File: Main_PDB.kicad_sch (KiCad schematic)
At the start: 124 parts, among them J1 Conn_01x02_MountingPin, J10 Conn_01x02_MountingPin, J12 Conn_01x02_MountingPin, J2 Conn_01x02_MountingPin, J3 Conn_01x02_MountingPin, J4 Conn_01x02_MountingPin, J5 Conn_01x02_MountingPin, J6 Conn_01x01_MountingPin, J7 Conn_01x01_MountingPin, J8 Conn_01x09_MountingPin, J9 Conn_01x03_MountingPin, Q1 PMOS, Q10 NMOS, Q14 NMOS, Q15 NMOS, Q2 NPN, Q7 NMOS, Q8 NMOS, Q9 NMOS, U1 LRM36015, U10 LM5148RGYR, U11 ACS758LCB-100U-PFF-T, U12 TPS48110AQDGXRQ1, U13 LM5148RGYR, U14 UCC27511DBVR, U2 ACS758LCB-100U-PFF-T, U4 ACS758LCB-100U-PFF-T, U5 ACS758LCB-100U-PFF-T, U6 ACS758LCB-100U-PFF-T, U8 ACS758LCB-100U-PFF-T, U9 ACS758LCB-100U-PFF-T

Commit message: Changed 48->24 to 48->12
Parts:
- C14: value 30u -> 83u
- C2: value 15u -> 285u
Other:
- moved on the sheet: D7
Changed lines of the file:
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@@
 	)
 	(junction
-		(at 505.46 388.62)
+		(at 166.37 243.84)
 		(diameter 0)
 		(color 0 0 0 0)
 	)
 	(junction
-		(at 166.37 243.84)
+		(at 504.19 388.62)
 		(diameter 0)
 		(color 0 0 0 0)
@@
 	(wire
 		(pts
-			(xy 505.46 388.62) (xy 510.54 388.62)
-		)
-		(stroke
-			(width 0)
-			(type default)
-		)
-	)
-	(wire
-		(pts
 			(xy 64.77 138.43) (xy 64.77 114.3)
 		)
@@
 	(wire
 		(pts
-			(xy 499.11 388.62) (xy 505.46 388.62)
+			(xy 499.11 388.62) (xy 504.19 388.62)
 		)
 		(stroke
@@
 	(wire
 		(pts
+			(xy 504.19 388.62) (xy 510.54 388.62)
+		)
+		(stroke
+			(width 0)
+			(type default)
+		)
+	)
+	(wire
+		(pts
 			(xy 34.29 99.06) (xy 68.58 99.06)
 		)
@@
 	(symbol
 		(lib_id "Device:D_Zener")
-		(at 505.46 384.81 90)
+		(at 504.19 384.81 90)
 		(unit 1)
 		(body_style 1)
@@
 		(dnp no)
 		(property "Reference" "D7"
-			(at 509.27 382.27 90)
+			(at 508 382.27 90)
 			(show_name no)
 			(do_not_autoplace no)
@@
 		)
 		(property "Value" "TVS"
-			(at 509.27 384.81 90)
+			(at 508 384.81 90)
 			(show_name no)
 			(do_not_autoplace no)
@@
 		)
 		(property "Footprint" ""
-			(at 505.46 384.81 0)
+			(at 504.19 384.81 0)
 			(hide yes)
 			(show_name no)
@@
 		)
 		(property "Datasheet" ""
-			(at 505.46 384.81 0)
+			(at 504.19 384.81 0)
 			(hide yes)
 			(show_name no)
@@
 		)
 		(property "Description" "Zener diode"
-			(at 505.46 384.81 0)
+			(at 504.19 384.81 0)
 			(hide yes)
 			(show_name no)
@@
 	(symbol
 		(lib_id "power:GND")
-		(at 505.46 381 180)
+		(at 504.19 381 180)
 		(unit 1)
 		(body_style 1)
@@
 		(fields_autoplaced yes)
 		(property "Reference" "#PWR054"
-			(at 505.46 374.65 0)
+			(at 504.19 374.65 0)
 			(hide yes)
 			(show_name no)
@@
 		)
 		(property "Value" "GND"
-			(at 505.4601 377.19 90)
+			(at 504.1901 377.19 90)
 			(show_name no)
 			(do_not_autoplace no)
@@
 		)
 		(property "Footprint" ""
-			(at 505.46 381 0)
+			(at 504.19 381 0)
 			(hide yes)
 			(show_name no)
@@
 		)
 		(property "Datasheet" ""
-			(at 505.46 381 0)
+			(at 504.19 381 0)
 			(hide yes)
 			(show_name no)
@@
 		)
 		(property "Description" "Power symbol creates a global label with name \"GND\" , ground"
-			(at 505.46 381 0)
+			(at 504.19 381 0)
 			(hide yes)
 			(show_name no)
@@
 			)
 		)
-		(property "Value" "15u"
+		(property "Value" "285u"
 			(at 335.28 351.7899 0)
 			(show_name no)
@@
 			)
 		)
-		(property "Value" "30u"
+		(property "Value" "83u"
 			(at 502.92 393.6999 0)
 			(show_name no)
@@
 		(dnp no)
 		(property "Reference" "Q7"
-			(at 85.09 40.64 90)
+			(at 85.344 54.356 90)
 			(show_name no)
 			(do_not_autoplace no)

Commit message: Format change
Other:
- note added: "48V to 12V buck + current sensor"
- note removed: "48V to 24V buck + current sensor"
- moved on the sheet: C1, C10, C11, C12, C13, C14, C19, C2, C20, C21, C22, C23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

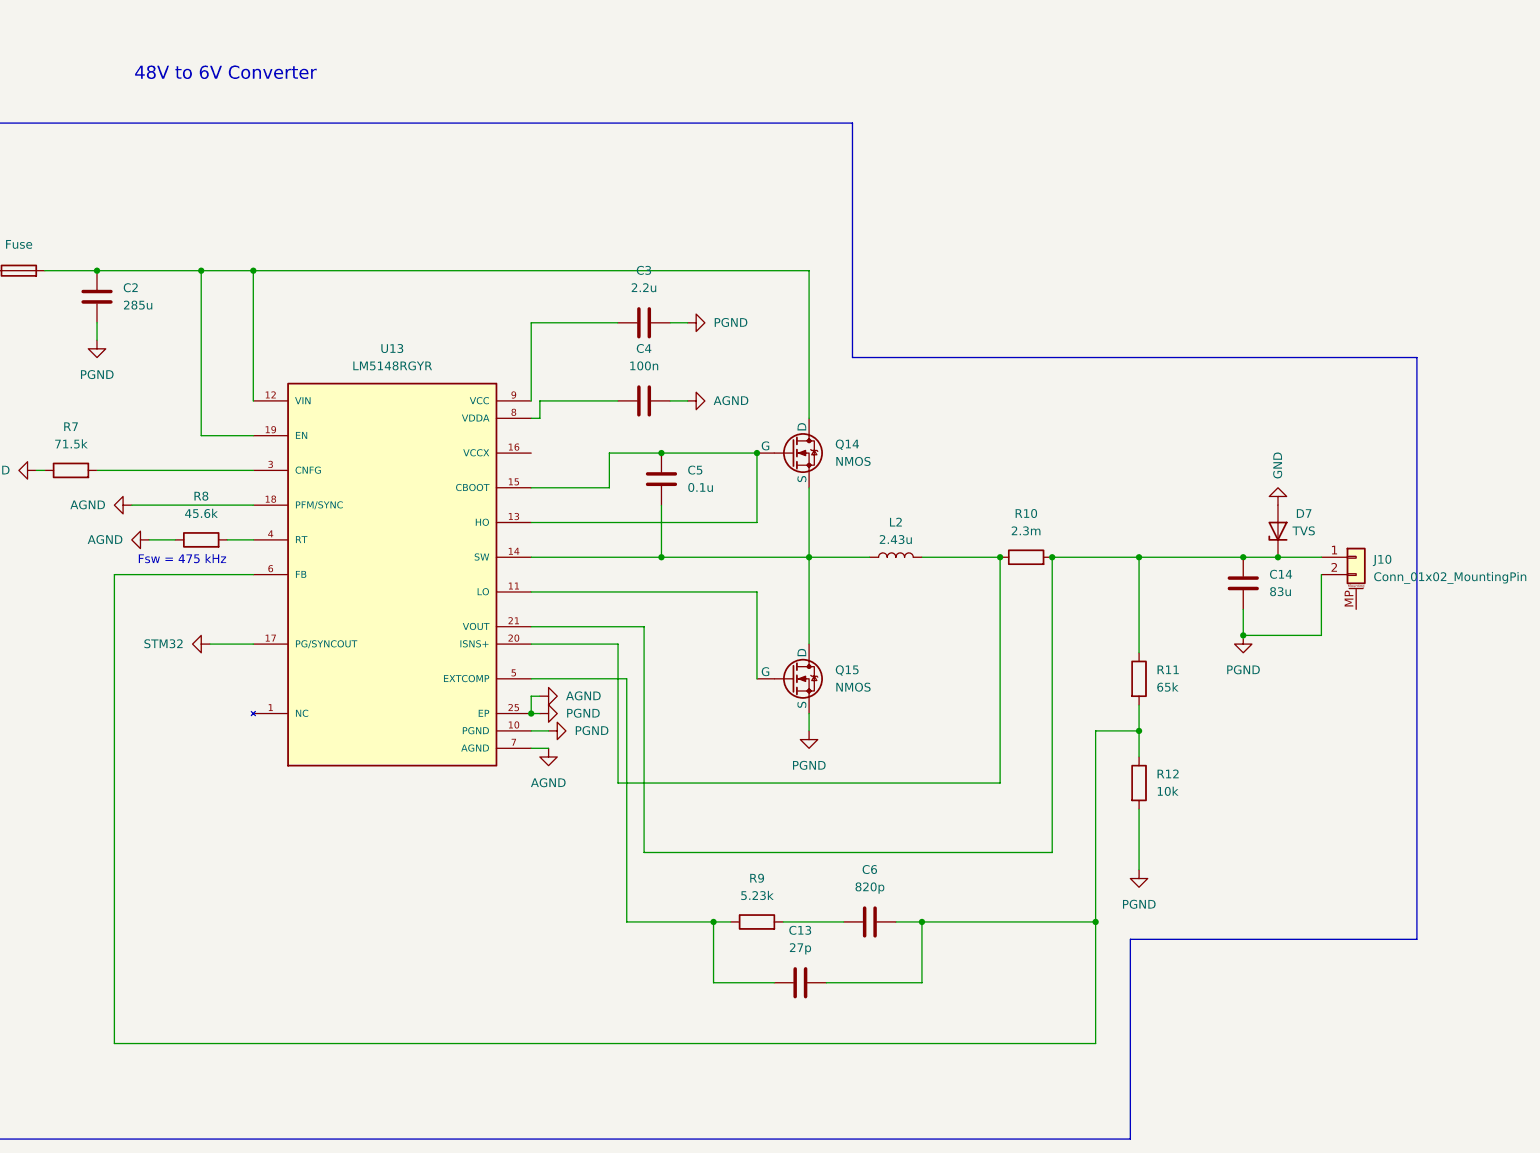
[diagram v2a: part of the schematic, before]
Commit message: updated component values for 6v convert
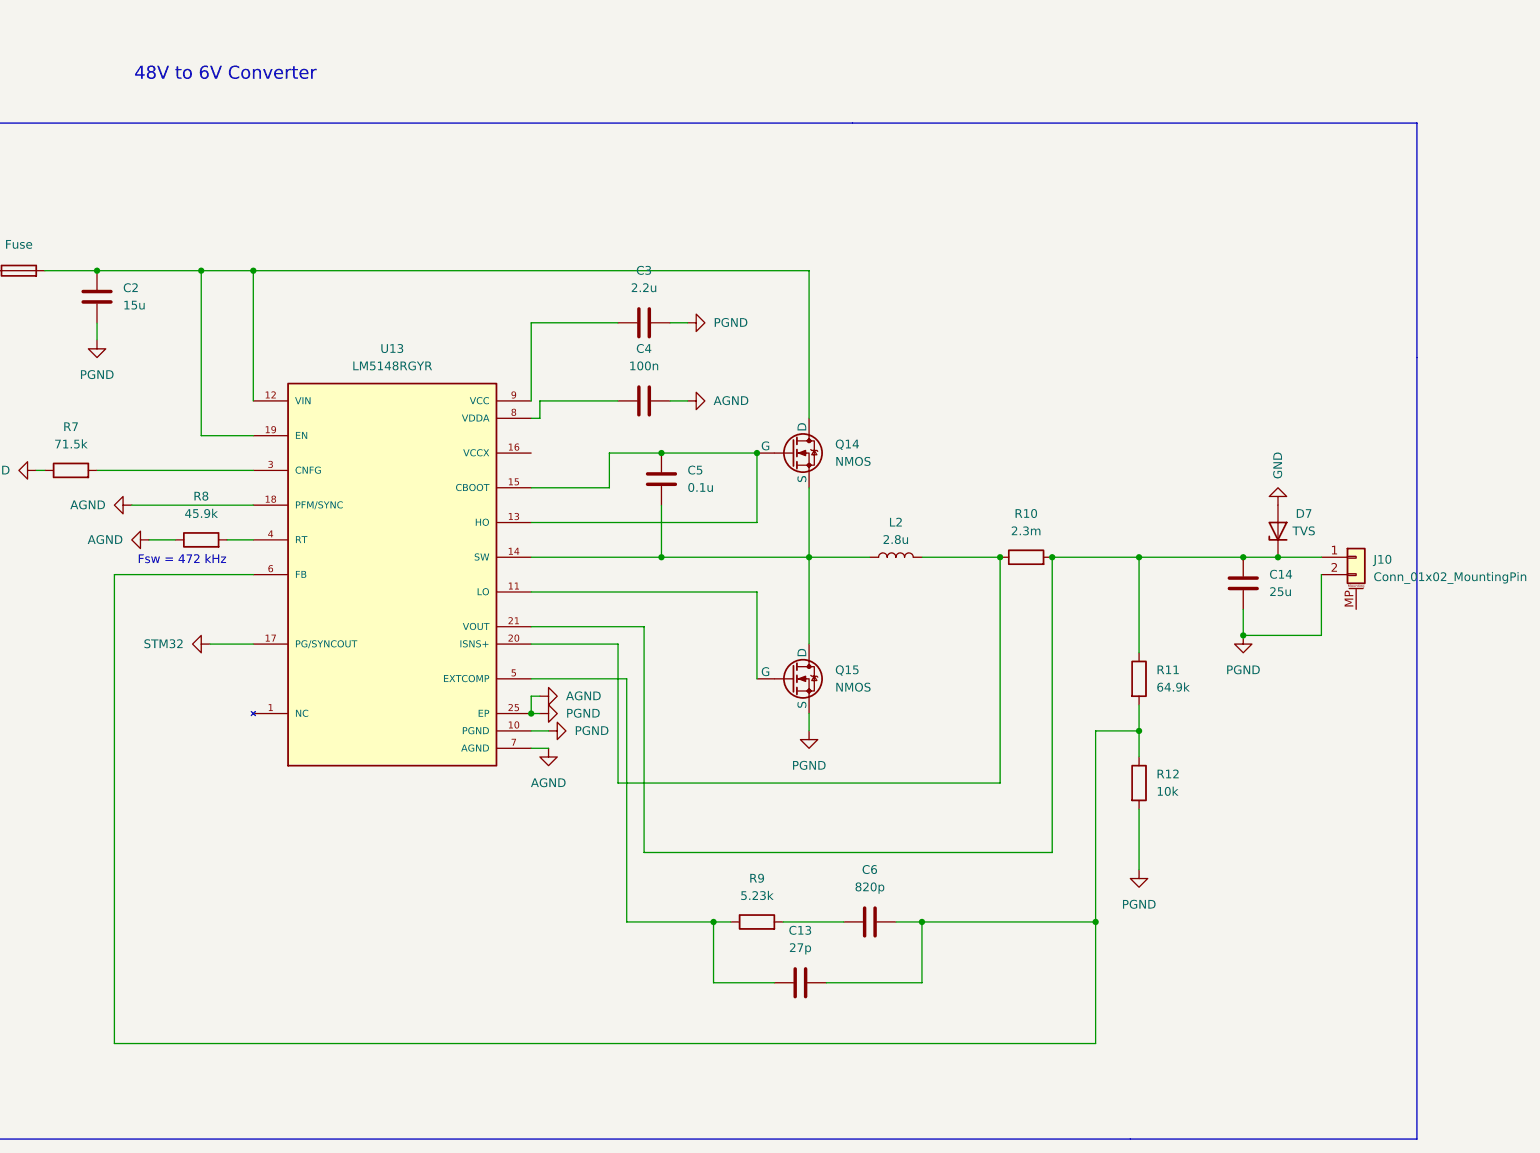
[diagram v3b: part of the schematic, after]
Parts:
- C14: value 83u -> 25u
- C2: value 285u -> 15u
- L2: value 2.43u -> 2.8u
- R11: value 65k -> 64.9k
- R8: value 45.6k -> 45.9k
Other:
- note added: "Fsw = 472 kHz"
- note removed: "Fsw = 475 kHz"
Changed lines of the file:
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@@
 		)
 	)
-	(text "Fsw = 475 kHz"
+	(text "Fsw = 472 kHz"
 		(exclude_from_sim no)
 		(at 553.466 399.288 0)
@@
 	(polyline
 		(pts
-			(xy 692.15 483.87) (xy 692.15 454.66)
+			(xy 692.15 483.87) (xy 692.15 483.87)
 		)
 		(stroke
@@
 	(polyline
 		(pts
-			(xy 692.15 454.66) (xy 734.06 454.66)
+			(xy 692.15 483.87) (xy 734.06 483.87)
 		)
 		(stroke
@@
 	(polyline
 		(pts
-			(xy 734.06 369.57) (xy 651.51 369.57)
+			(xy 734.06 369.57) (xy 734.06 335.28)
 		)
 		(stroke
@@
 	(polyline
 		(pts
-			(xy 734.06 454.66) (xy 734.06 369.57)
+			(xy 734.06 483.87) (xy 734.06 369.57)
 		)
 		(stroke
@@
 	(polyline
 		(pts
-			(xy 651.51 369.57) (xy 651.51 335.28)
+			(xy 734.06 335.28) (xy 651.51 335.28)
 		)
 		(stroke
@@
 			)
 		)
-		(property "Value" "65k"
+		(property "Value" "64.9k"
 			(at 695.96 417.8299 0)
 			(show_name no)
@@
 			)
 		)
-		(property "Value" "45.6k"
+		(property "Value" "45.9k"
 			(at 556.26 392.43 90)
 			(show_name no)
@@
 			)
 		)
-		(property "Value" "2.43u"
+		(property "Value" "2.8u"
 			(at 657.86 396.24 90)
 			(show_name no)
@@
 			)
 		)
-		(property "Value" "285u"
+		(property "Value" "15u"
 			(at 544.83 361.9499 0)
 			(show_name no)
@@
 			)
 		)
-		(property "Value" "83u"
+		(property "Value" "25u"
 			(at 712.47 403.8599 0)
 			(show_name no)

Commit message: updated grounds for converters, need to double check grounds for current sense. Did not adjust grounds on actuators/precharge. Added pull up resistor on 6v PG output.
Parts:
- added R4: PullUpRes, symbol Device:R
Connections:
- net AGND: now also C26.2, C27.2, C28.2, C29.2, C30.2, C31.2, C33.2, C38.2, C39.2, C40.2, C41.2, C45.2, C46.2, C47.2, C48.2, C49.2, CHF1.2, CHF2.2, CIN1.2, COUT1.2, COUT2.2, CVCC1.1, J1.2 (Pin_2), J12.2 (Pin_2), Q9.3 (S), R17.1, R18.1, R21.2, RFBB1.1, U1.1 (PGND), U1.11 (PGND), U1.6 (AGND), U10.10 (PGND), U10.16 (VCCX), U10.17 (PG/SYNCOUT), U10.18 (PFM/SYNC), U10.25 (EP), U10.7 (AGND), U11.2 (GND), U9.2 (GND)
- net GND: no longer C26.2, C27.2, C28.2, C29.2, C30.2, C31.2, C38.2, C39.2, C40.2, C41.2, C43.2, C44.2, C45.2, C46.2, C48.2, C49.2, CHF1.2, CHF2.2, CIN1.2, COUT1.2, COUT2.2, CVCC1.1, J1.2 (Pin_2), J12.2 (Pin_2), Q9.3 (S), R17.1, R18.1, R21.2, RFBB1.1, U1.1 (PGND), U1.11 (PGND), U1.6 (AGND), U10.10 (PGND), U10.16 (VCCX), U10.17 (PG/SYNCOUT), U10.18 (PFM/SYNC), U10.25 (EP), U10.7 (AGND)
- net GND1: no longer C33.2, C47.2, U11.2 (GND), U9.2 (GND)
- net STM32: now also R4.1; no longer U13.17 (PG/SYNCOUT)
- net at R20.2, R21.1, U10.6 (FB): now also C43.2, C44.2
- new net: R4.2, U13.17 (PG/SYNCOUT)
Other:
- moved on the sheet: R7

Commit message: changed ground for ext comp circuit
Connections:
- net AGND: now also C13.2, C43.2, C44.2, C6.2
- net at R11.2, R12.1, U13.6 (FB): no longer C13.2, C6.2
- net at R20.2, R21.1, U10.6 (FB): no longer C43.2, C44.2
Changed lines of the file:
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@@
 	)
 	(junction
+		(at 213.36 435.61)
+		(diameter 0)
+		(color 0 0 0 0)
+	)
+	(junction
 		(at 185.42 176.53)
 		(diameter 0)
@@
 	)
 	(junction
-		(at 260.35 443.23)
-		(diameter 0)
-		(color 0 0 0 0)
-	)
-	(junction
 		(at 196.85 440.69)
 		(diameter 0)
@@
 	)
 	(junction
-		(at 213.36 435.61)
-		(diameter 0)
-		(color 0 0 0 0)
-	)
-	(junction
 		(at 638.81 148.59)
 		(diameter 0)
@@
 	)
 	(junction
-		(at 687.07 452.12)
-		(diameter 0)
-		(color 0 0 0 0)
-	)
-	(junction
 		(at 234.95 265.43)
 		(diameter 0)
@@
 	(wire
 		(pts
-			(xy 226.06 435.61) (xy 226.06 448.31)
-		)
-		(stroke
-			(width 0)
-			(type default)
-		)
-	)
-	(wire
-		(pts
 			(xy 161.29 82.55) (xy 161.29 110.49)
 		)
@@
 	(wire
 		(pts
-			(xy 255.27 443.23) (xy 260.35 443.23)
-		)
-		(stroke
-			(width 0)
-			(type default)
-		)
-	)
-	(wire
-		(pts
 			(xy 295.91 471.17) (xy 295.91 464.82)
 		)
@@
 	(wire
 		(pts
+			(xy 213.36 435.61) (xy 217.17 435.61)
+		)
+		(stroke
+			(width 0)
+			(type default)
+		)
+	)
+	(wire
+		(pts
 			(xy 217.17 402.59) (xy 217.17 397.51)
 		)
@@
 	(wire
 		(pts
-			(xy 260.35 443.23) (xy 260.35 444.5)
-		)
-		(stroke
-			(width 0)
-			(type default)
-		)
-	)
-	(wire
-		(pts
 			(xy 195.58 412.75) (xy 226.06 412.75)
 		)
@@
 	(wire
 		(pts
-			(xy 226.06 448.31) (xy 255.27 448.31)
-		)
-		(stroke
-			(width 0)
-			(type default)
-		)
-	)
-	(wire
-		(pts
 			(xy 570.23 109.22) (xy 574.04 109.22)
 		)
@@
 	(wire
 		(pts
-			(xy 661.67 452.12) (xy 687.07 452.12)
+			(xy 661.67 452.12) (xy 666.75 452.12)
 		)
 		(stroke
@@
 	(wire
 		(pts
-			(xy 260.35 441.96) (xy 260.35 443.23)
+			(xy 260.35 441.96) (xy 260.35 444.5)
 		)
 		(stroke
@@
 	(wire
 		(pts
-			(xy 687.07 452.12) (xy 687.07 469.9)
-		)
-		(stroke
-			(width 0)
-			(type default)
-		)
-	)
-	(wire
-		(pts
 			(xy 186.69 144.78) (xy 186.69 170.18)
 		)
@@
 	(wire
 		(pts
-			(xy 255.27 448.31) (xy 255.27 443.23)
-		)
-		(stroke
-			(width 0)
-			(type default)
-		)
-	)
-	(wire
-		(pts
 			(xy 623.57 391.16) (xy 623.57 398.78)
 		)
@@
 	(wire
 		(pts
-			(xy 687.07 424.18) (xy 687.07 452.12)
+			(xy 687.07 424.18) (xy 687.07 469.9)
 		)
 		(stroke
@@
 	(wire
 		(pts
-			(xy 213.36 435.61) (xy 226.06 435.61)
-		)
-		(stroke
-			(width 0)
-			(type default)
-		)
-	)
-	(wire
-		(pts
 			(xy 190.5 257.81) (xy 190.5 264.16)
 		)
@@
 	(symbol
 		(lib_id "power:GND")
+		(at 217.17 435.61 90)
+		(unit 1)
+		(body_style 1)
+		(exclude_from_sim no)
+		(in_bom yes)
+		(on_board yes)
+		(in_pos_files yes)
+		(dnp no)
+		(fields_autoplaced yes)
+		(property "Reference" "#PWR062"
+			(at 223.52 435.61 0)
+			(hide yes)
+			(show_name no)
+			(do_not_autoplace no)
+			(effects
+				(font
+					(size 1.27 1.27)
+				)
+			)
+		)
+		(property "Value" "PGND"
+			(at 220.98 435.6099 90)
+			(show_name no)
+			(do_not_autoplace no)
+			(effects
+				(font
+					(size 1.27 1.27)
+				)
+				(justify right)
+			)
+		)
+		(property "Footprint" ""
+			(at 217.17 435.61 0)
+			(hide yes)
+			(show_name no)
+			(do_not_autoplace no)
+			(effects
+				(font
+					(size 1.27 1.27)
+				)
+			)
+		)
+		(property "Datasheet" ""
+			(at 217.17 435.61 0)
+			(hide yes)
+			(show_name no)
+			(do_not_autoplace no)
+			(effects
+				(font
+					(size 1.27 1.27)
+				)
+			)
+		)
+		(property "Description" "Power symbol creates a global label with name \"GND\" , ground"
+			(at 217.17 435.61 0)
+			(hide yes)
+			(show_name no)
+			(do_not_autoplace no)
+			(effects
+				(font
+					(size 1.27 1.27)
+				)
+			)
+		)
+		(pin "1"
+		)
+		(instances
+			(project "Main_PDB"
+				(path "/b0f96dc2-0eeb-4c9a-9b54-b0ba45b68ce7"
+					(reference "#PWR062")
+					(unit 1)
+				)
+			)
+		)
+	)
+	(symbol
+		(lib_id "power:GND")
 		(at 687.07 195.58 270)
 		(unit 1)
@@
 					(unit 1)
 				)
+			)
+		)
+	)
+	(symbol
+		(lib_id "power:GND")
+		(at 666.75 452.12 90)
+		(unit 1)
+		(body_style 1)
+		(exclude_from_sim no)
+		(in_bom yes)
+		(on_board yes)
+		(in_pos_files yes)
+		(dnp no)
+		(fields_autoplaced yes)
+		(property "Reference" "#PWR065"
+			(at 673.1 452.12 0)
+			(hide yes)
+			(show_name no)
+			(do_not_autoplace no)
+			(effects
+				(font
+					(size 1.27 1.27)
+				)
+			)
+		)
+		(property "Value" "PGND"
+			(at 670.56 452.1199 90)
+			(show_name no)
+			(do_not_autoplace no)
+			(effects
+				(font
+					(size 1.27 1.27)
+				)
+				(justify right)
+			)
+		)
+		(property "Footprint" ""
+			(at 666.75 452.12 0)
+			(hide yes)
+			(show_name no)
+			(do_not_autoplace no)
+			(effects
+				(font
+					(size 1.27 1.27)
+				)
+			)
+		)
+		(property "Datasheet" ""
+			(at 666.75 452.12 0)
+			(hide yes)
+			(show_name no)
+			(do_not_autoplace no)
+			(effects
+				(font
+					(size 1.27 1.27)
+				)
+			)
+		)
+		(property "Description" "Power symbol creates a global label with name \"GND\" , ground"
+			(at 666.75 452.12 0)
+			(hide yes)
+			(show_name no)
+			(do_not_autoplace no)
+			(effects
+				(font
+					(size 1.27 1.27)
+				)
+			)
+		)
+		(pin "1"
+		)
+		(instances
+			(project "Main_PDB"
+				(path "/b0f96dc2-0eeb-4c9a-9b54-b0ba45b68ce7"
+					(reference "#PWR065")
+					(unit 1)
+				)

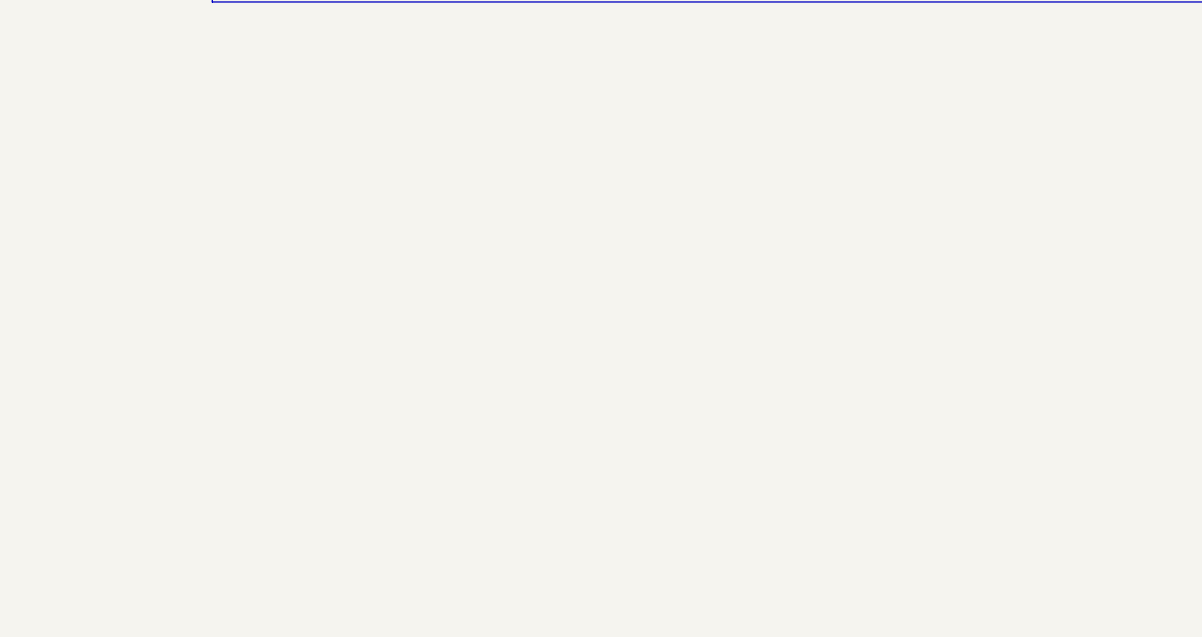
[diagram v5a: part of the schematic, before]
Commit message: added thermistors in lower left hand side, exact values, quantity,and need for more specific measurement will be determined during testing/tracing.
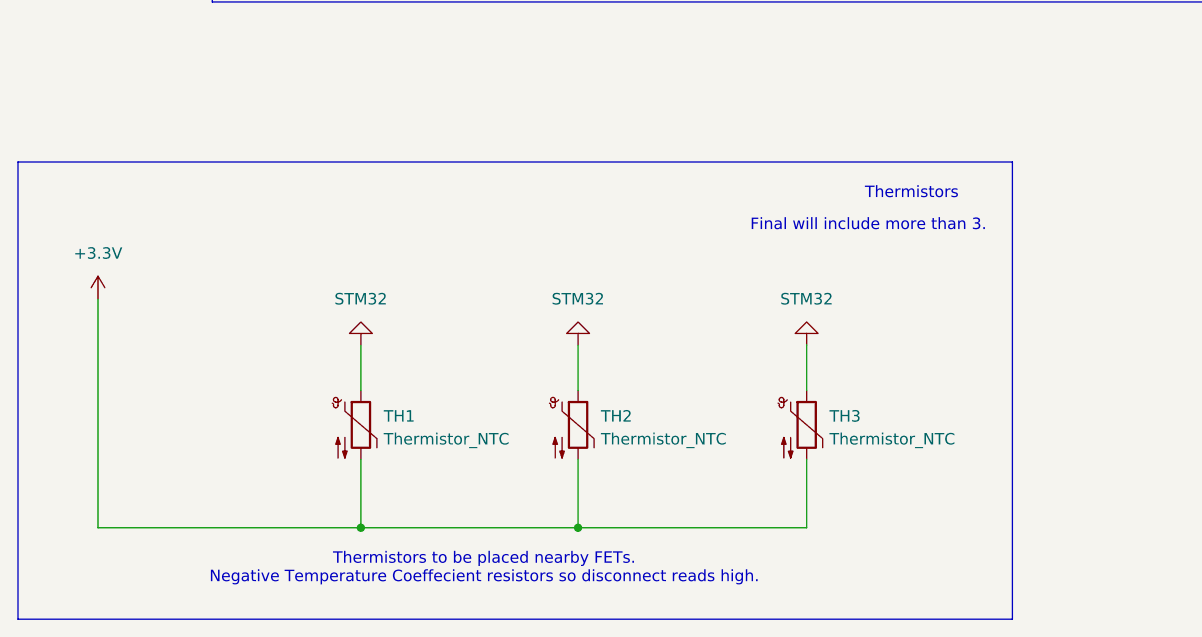
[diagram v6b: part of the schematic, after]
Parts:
- added TH1, TH2, TH3: Thermistor_NTC, symbol Device:Thermistor_NTC
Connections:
- net +3.3V: now also TH1.2, TH2.2, TH3.2
- net STM32: now also TH1.1, TH2.1, TH3.1
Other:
- note added: "Final will include more than 3."
- note added: "Thermistors"
- note added: "Thermistors to be placed nearby FETs. Negative Temperature Coeffecient resistors so disconnect reads high."
